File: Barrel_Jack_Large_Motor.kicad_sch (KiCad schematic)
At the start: 9 parts, among them J15 Barrel_Jack, J16 Barrel_Jack, J17 Barrel_Jack, J18 Barrel_Jack, J19 Barrel_Jack, J20 Barrel_Jack, U27 L298N, U28 L298N, U29 L298N

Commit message: motor layout
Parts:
- added F29, F30, F31, F32, F33, F34, F35, F36: Fuse, symbol Device:Fuse
- added J36, J37: Barrel_Jack, symbol Connector:Barrel_Jack
- added U10, U38: PCF8574ATS, Package_SO:SSOP-20_4.4x6.5mm_P0.65mm, symbol Interface_Expansion:PCF8574ATS
- added U37: L298N, Package_TO_SOT_THT:TO-220-15_P2.54x2.54mm_StaggerOdd_Lead4.58mm_Vertical, symbol Driver_Motor:L298N
- added U39: PCA9685PW, Package_SO:TSSOP-28_4.4x9.7mm_P0.65mm, symbol Driver_LED:PCA9685PW
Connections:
- net at J15.1: now also F30.1; no longer U27.14 (OUT4)
- net at J17.1: now also F31.1; no longer U28.14 (OUT4)
- net at U28.10 (IN3): now also U10.19 (P6)
- net at U28.11 (EnB): now also U39.9 (LED3)
- net at U28.12 (IN4): now also U10.20 (P7)
- net at U28.3 (OUT2): now also F32.2; no longer J18.1
- net at U28.5 (IN1): now also U10.16 (P4)
- net at U28.6 (EnA): now also U39.8 (LED2)
- net at U28.7 (IN2): now also U10.17 (P5)
- net at J19.1: now also F34.1; no longer U29.14 (OUT4)
- net at U29.10 (IN3): now also U38.12 (P2)
- net at U29.11 (EnB): now also U39.11 (LED5)
- net at U29.12 (IN4): now also U38.14 (P3)
- net at J20.1: now also F33.1; no longer U29.3 (OUT2)
- net at U29.5 (IN1): now also U38.10 (P0)
- net at U29.6 (EnA): now also U39.10 (LED4)
- net at U29.7 (IN2): now also U38.11 (P1)
- net at J16.1: now also F29.1; no longer U27.3 (OUT2)
- net at U27.10 (IN3): now also U10.12 (P2)
- net at U27.11 (EnB): now also U39.7 (LED1)
- net at U27.12 (IN4): now also U10.14 (P3)
- net at U27.5 (IN1): now also U10.10 (P0)
- net at U27.6 (EnA): now also U39.6 (LED0)
- net at U27.7 (IN2): now also U10.11 (P1)
- new net: F36.1, J36.1
- new net: J36.2, U37.13 (OUT3)
- new net: F36.2, U37.14 (OUT4)
- new net: U37.10 (IN3), U38.19 (P6)
- new net: U37.11 (EnB), U39.13 (LED7)
- new net: U37.12 (IN4), U38.20 (P7)
- new net: J37.2, U37.2 (OUT1)
- new net: F35.2, U37.3 (OUT2)
- new net: U37.5 (IN1), U38.16 (P4)
- new net: U37.6 (EnA), U39.12 (LED6)
- new net: U37.7 (IN2), U38.17 (P5)
- new net: F29.2, U27.3 (OUT2)
- new net: F31.2, U28.14 (OUT4)
- new net: F33.2, U29.3 (OUT2)
- new net: F32.1, J18.1
- new net: F30.2, U27.14 (OUT4)
- new net: F34.2, U29.14 (OUT4)
- new net: F35.1, J37.1
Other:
- moved on the sheet: J15, J16, J17, J18, J19, J20, U27, U28, U29

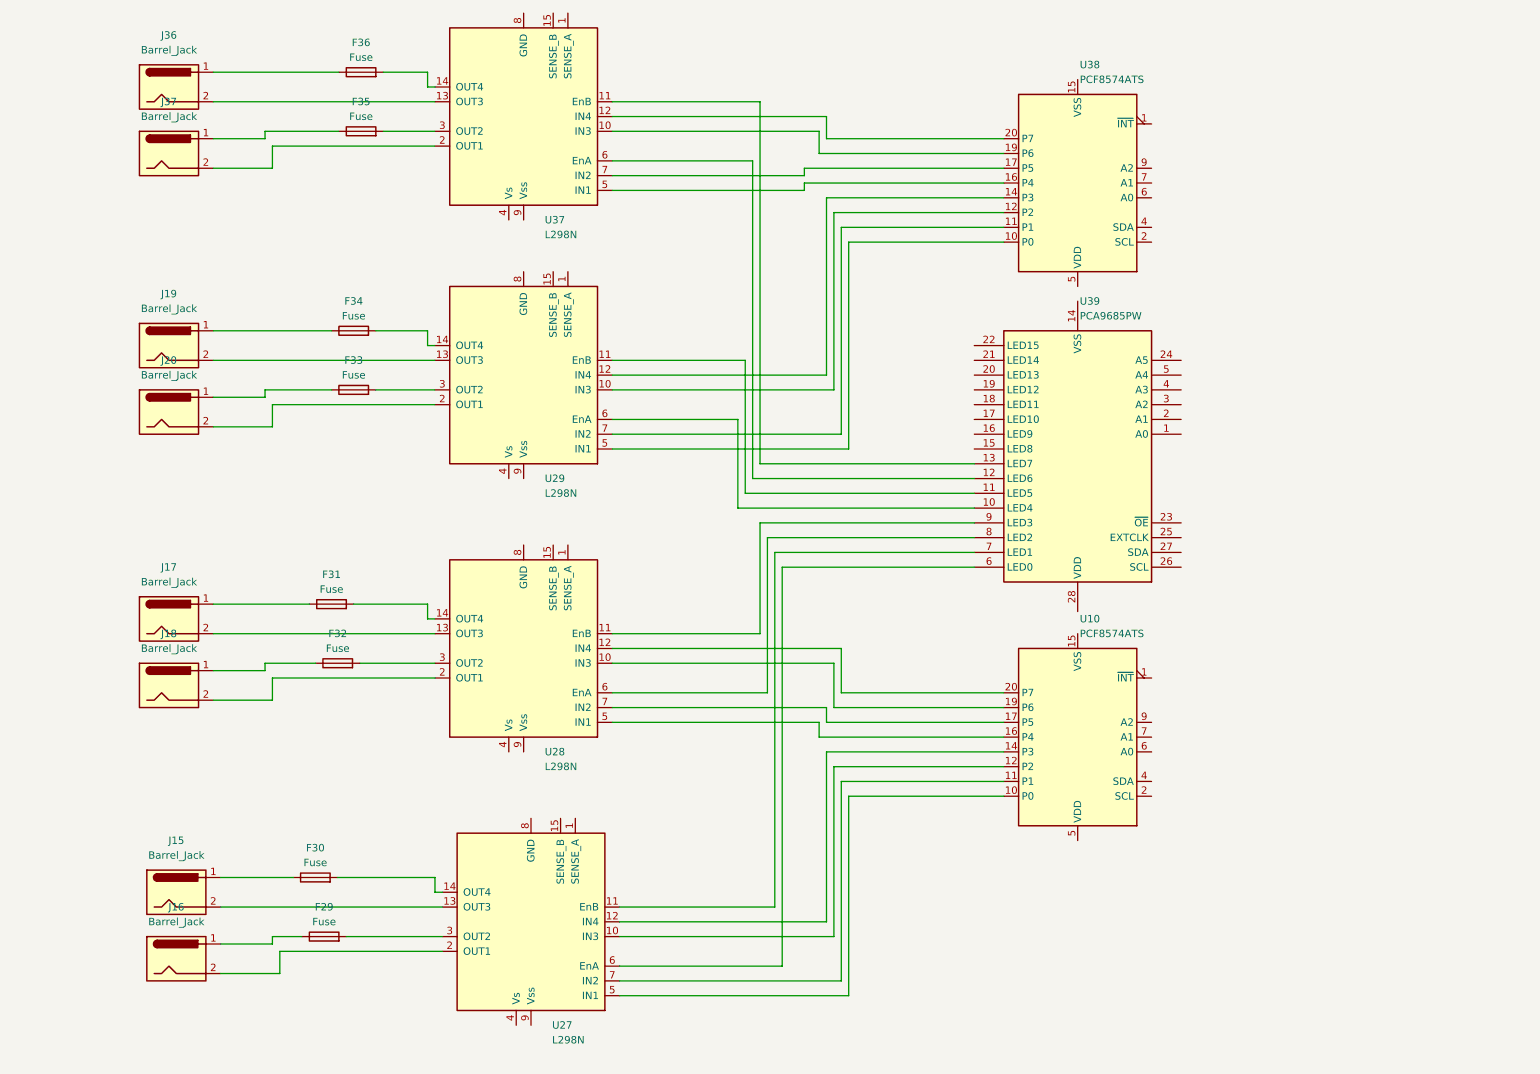
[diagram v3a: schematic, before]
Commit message: placeholders for ethernet and relay inputs
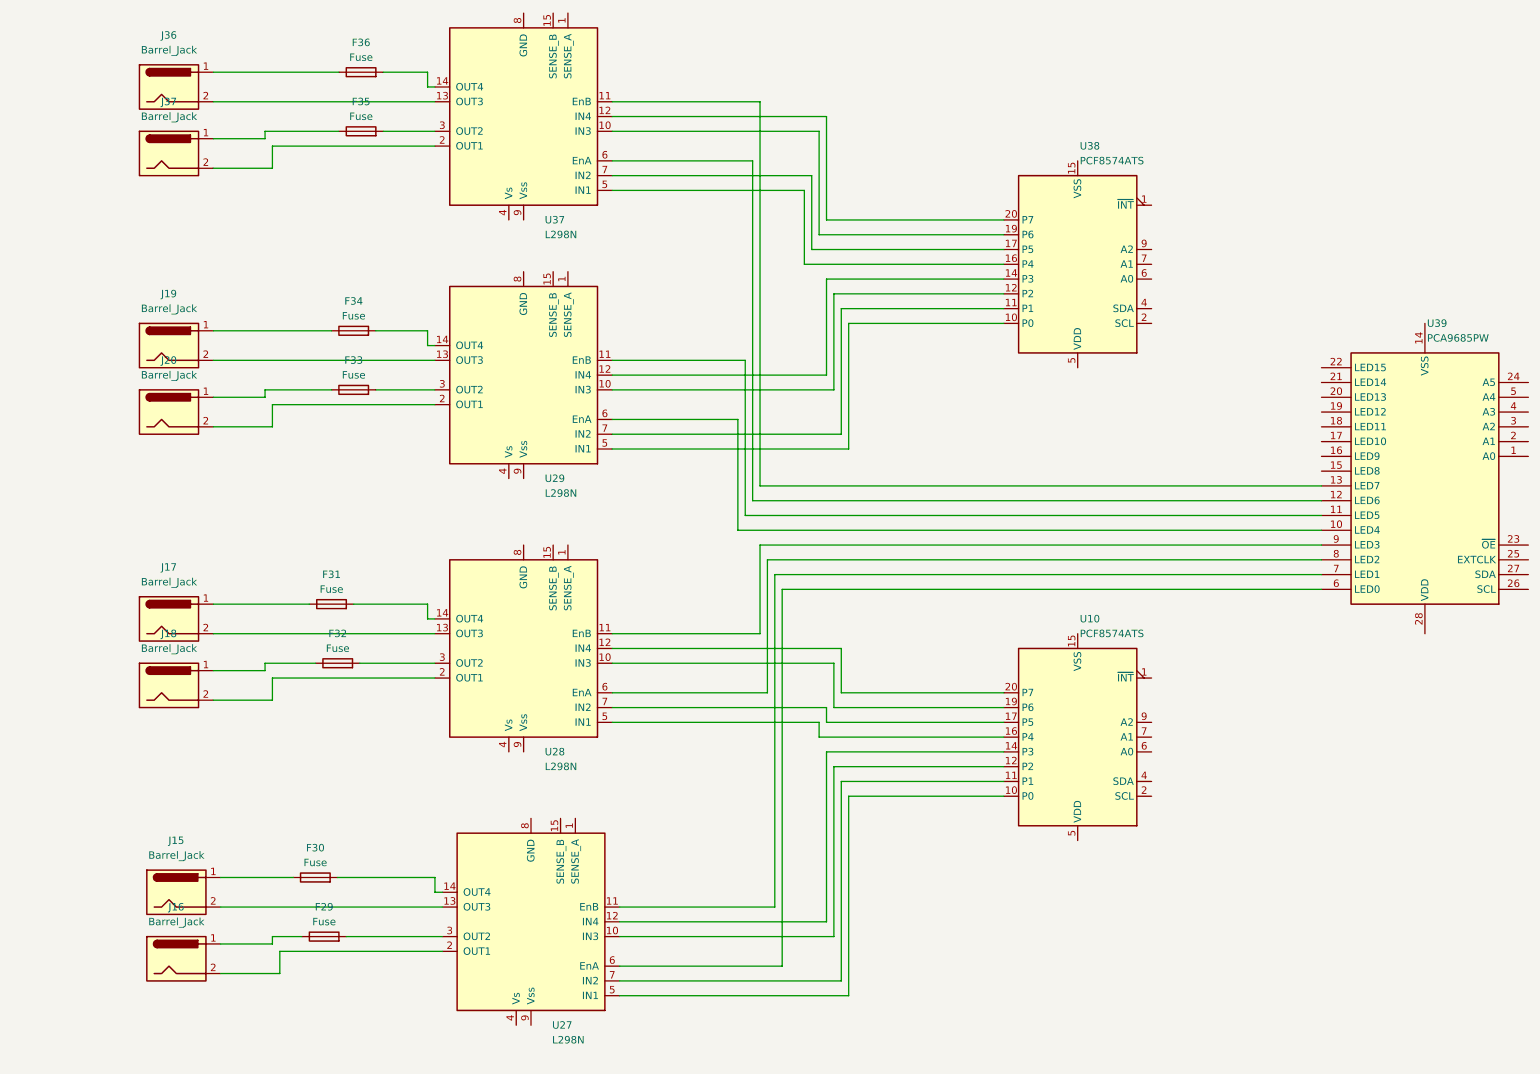
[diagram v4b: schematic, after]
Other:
- moved on the sheet: U38, U39
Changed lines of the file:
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@@
 (kicad_sch (version 20230121) (generator eeschema)
   (paper "A4")
-  (wire (pts (xy 160.02 54.61) (xy 160.02 90.17))
-    (stroke (width 0) (type default))
-  )
-  (wire (pts (xy 120.65 45.72) (xy 153.67 45.72))
-    (stroke (width 0) (type default))
-  )
-  (wire (pts (xy 182.88 107.95) (xy 147.32 107.95))
+  (wire (pts (xy 160.02 68.58) (xy 160.02 90.17))
+    (stroke (width 0) (type default))
+  )
+  (wire (pts (xy 120.65 45.72) (xy 154.94 45.72))
+    (stroke (width 0) (type default))
+  )
+  (wire (pts (xy 242.57 111.76) (xy 147.32 111.76))
     (stroke (width 0) (type default))
   )
@@
     (stroke (width 0) (type default))
   )
-  (wire (pts (xy 146.05 124.46) (xy 146.05 105.41))
+  (wire (pts (xy 146.05 124.46) (xy 146.05 109.22))
     (stroke (width 0) (type default))
   )
@@
     (stroke (width 0) (type default))
   )
-  (wire (pts (xy 149.86 113.03) (xy 149.86 181.61))
+  (wire (pts (xy 149.86 116.84) (xy 149.86 181.61))
     (stroke (width 0) (type default))
   )
@@
     (stroke (width 0) (type default))
   )
-  (wire (pts (xy 182.88 113.03) (xy 149.86 113.03))
-    (stroke (width 0) (type default))
-  )
-  (wire (pts (xy 187.96 46.99) (xy 153.67 46.99))
+  (wire (pts (xy 242.57 116.84) (xy 149.86 116.84))
+    (stroke (width 0) (type default))
+  )
+  (wire (pts (xy 153.67 60.96) (xy 153.67 48.26))
+    (stroke (width 0) (type default))
+  )
+  (wire (pts (xy 153.67 60.96) (xy 187.96 60.96))
     (stroke (width 0) (type default))
   )
@@
     (stroke (width 0) (type default))
   )
-  (wire (pts (xy 187.96 52.07) (xy 158.75 52.07))
+  (wire (pts (xy 187.96 66.04) (xy 158.75 66.04))
     (stroke (width 0) (type default))
   )
@@
     (stroke (width 0) (type default))
   )
-  (wire (pts (xy 146.05 95.25) (xy 146.05 33.02))
+  (wire (pts (xy 146.05 99.06) (xy 146.05 33.02))
     (stroke (width 0) (type default))
   )
@@
     (stroke (width 0) (type default))
   )
-  (wire (pts (xy 120.65 48.26) (xy 153.67 48.26))
-    (stroke (width 0) (type default))
-  )
   (wire (pts (xy 157.48 35.56) (xy 120.65 35.56))
     (stroke (width 0) (type default))
@@
     (stroke (width 0) (type default))
   )
-  (wire (pts (xy 187.96 54.61) (xy 160.02 54.61))
+  (wire (pts (xy 187.96 68.58) (xy 160.02 68.58))
     (stroke (width 0) (type default))
   )
@@
     (stroke (width 0) (type default))
   )
-  (wire (pts (xy 146.05 105.41) (xy 182.88 105.41))
+  (wire (pts (xy 146.05 109.22) (xy 242.57 109.22))
     (stroke (width 0) (type default))
   )
@@
     (stroke (width 0) (type default))
   )
-  (wire (pts (xy 187.96 41.91) (xy 156.21 41.91))
+  (wire (pts (xy 187.96 55.88) (xy 156.21 55.88))
     (stroke (width 0) (type default))
   )
@@
     (stroke (width 0) (type default))
   )
-  (wire (pts (xy 158.75 52.07) (xy 158.75 82.55))
-    (stroke (width 0) (type default))
-  )
-  (wire (pts (xy 157.48 49.53) (xy 157.48 80.01))
+  (wire (pts (xy 158.75 66.04) (xy 158.75 82.55))
+    (stroke (width 0) (type default))
+  )
+  (wire (pts (xy 157.48 63.5) (xy 157.48 80.01))
     (stroke (width 0) (type default))
   )
@@
     (stroke (width 0) (type default))
   )
-  (wire (pts (xy 148.59 110.49) (xy 182.88 110.49))
+  (wire (pts (xy 148.59 114.3) (xy 242.57 114.3))
     (stroke (width 0) (type default))
   )
@@
     (stroke (width 0) (type default))
   )
-  (wire (pts (xy 182.88 95.25) (xy 146.05 95.25))
+  (wire (pts (xy 242.57 99.06) (xy 146.05 99.06))
     (stroke (width 0) (type default))
   )
@@
     (stroke (width 0) (type default))
   )
-  (wire (pts (xy 142.24 102.87) (xy 142.24 87.63))
+  (wire (pts (xy 142.24 106.68) (xy 142.24 87.63))
     (stroke (width 0) (type default))
   )
@@
     (stroke (width 0) (type default))
   )
-  (wire (pts (xy 153.67 44.45) (xy 187.96 44.45))
-    (stroke (width 0) (type default))
-  )
-  (wire (pts (xy 144.78 97.79) (xy 182.88 97.79))
-    (stroke (width 0) (type default))
-  )
-  (wire (pts (xy 143.51 100.33) (xy 143.51 77.47))
+  (wire (pts (xy 154.94 58.42) (xy 187.96 58.42))
+    (stroke (width 0) (type default))
+  )
+  (wire (pts (xy 144.78 101.6) (xy 242.57 101.6))
+    (stroke (width 0) (type default))
+  )
+  (wire (pts (xy 143.51 104.14) (xy 143.51 77.47))
     (stroke (width 0) (type default))
   )
@@
     (stroke (width 0) (type default))
   )
-  (wire (pts (xy 161.29 92.71) (xy 161.29 57.15))
+  (wire (pts (xy 161.29 92.71) (xy 161.29 71.12))
     (stroke (width 0) (type default))
   )
@@
     (stroke (width 0) (type default))
   )
-  (wire (pts (xy 157.48 39.37) (xy 157.48 35.56))
+  (wire (pts (xy 157.48 53.34) (xy 157.48 35.56))
     (stroke (width 0) (type default))
   )
@@
     (stroke (width 0) (type default))
   )
+  (wire (pts (xy 153.67 48.26) (xy 120.65 48.26))
+    (stroke (width 0) (type default))
+  )
   (wire (pts (xy 62.23 44.45) (xy 52.07 44.45))
     (stroke (width 0) (type default))
@@
     (stroke (width 0) (type default))
   )
-  (wire (pts (xy 161.29 57.15) (xy 187.96 57.15))
-    (stroke (width 0) (type default))
-  )
-  (wire (pts (xy 148.59 171.45) (xy 148.59 110.49))
-    (stroke (width 0) (type default))
-  )
-  (wire (pts (xy 144.78 43.18) (xy 144.78 97.79))
+  (wire (pts (xy 161.29 71.12) (xy 187.96 71.12))
+    (stroke (width 0) (type default))
+  )
+  (wire (pts (xy 148.59 171.45) (xy 148.59 114.3))
+    (stroke (width 0) (type default))
+  )
+  (wire (pts (xy 144.78 43.18) (xy 144.78 101.6))
     (stroke (width 0) (type default))
   )
@@
     (stroke (width 0) (type default))
   )
-  (wire (pts (xy 153.67 48.26) (xy 153.67 46.99))
-    (stroke (width 0) (type default))
-  )
   (wire (pts (xy 88.9 30.48) (xy 90.17 30.48))
     (stroke (width 0) (type default))
   )
-  (wire (pts (xy 187.96 49.53) (xy 157.48 49.53))
-    (stroke (width 0) (type default))
-  )
-  (wire (pts (xy 153.67 45.72) (xy 153.67 44.45))
+  (wire (pts (xy 187.96 63.5) (xy 157.48 63.5))
     (stroke (width 0) (type default))
   )
@@
     (stroke (width 0) (type default))
   )
-  (wire (pts (xy 147.32 107.95) (xy 147.32 134.62))
+  (wire (pts (xy 147.32 111.76) (xy 147.32 134.62))
     (stroke (width 0) (type default))
   )
@@
     (stroke (width 0) (type default))
   )
-  (wire (pts (xy 142.24 102.87) (xy 182.88 102.87))
+  (wire (pts (xy 142.24 106.68) (xy 242.57 106.68))
     (stroke (width 0) (type default))
   )
@@
     (stroke (width 0) (type default))
   )
-  (wire (pts (xy 182.88 100.33) (xy 143.51 100.33))
+  (wire (pts (xy 242.57 104.14) (xy 143.51 104.14))
     (stroke (width 0) (type default))
   )
@@
     (stroke (width 0) (type default))
   )
+  (wire (pts (xy 154.94 45.72) (xy 154.94 58.42))
+    (stroke (width 0) (type default))
+  )
   (wire (pts (xy 146.05 33.02) (xy 120.65 33.02))
     (stroke (width 0) (type default))
@@
     (stroke (width 0) (type default))
   )
-  (wire (pts (xy 187.96 39.37) (xy 157.48 39.37))
+  (wire (pts (xy 187.96 53.34) (xy 157.48 53.34))
     (stroke (width 0) (type default))
   )
@@
     (stroke (width 0) (type default))
   )
-  (wire (pts (xy 156.21 41.91) (xy 156.21 38.1))
+  (wire (pts (xy 156.21 55.88) (xy 156.21 38.1))
     (stroke (width 0) (type default))
   )
@@
     )
   )
-  (symbol (lib_id "Driver_LED:PCA9685PW") (at 200.66 95.25 180) (unit 1)
-    (in_bom yes) (on_board yes) (dnp no) (fields_autoplaced)
-    (property "Reference" "U39" (at 201.0059 67.31 0)
-      (effects (font (size 1.27 1.27)) (justify right))
-    )
-    (property "Value" "PCA9685PW" (at 201.0059 69.85 0)
-      (effects (font (size 1.27 1.27)) (justify right))
-    )
-    (property "Footprint" "Package_SO:TSSOP-28_4.4x9.7mm_P0.65mm" (at 200.025 70.485 0)
+  (symbol (lib_id "Driver_LED:PCA9685PW") (at 260.35 99.06 180) (unit 1)
+    (in_bom yes) (on_board yes) (dnp no) (fields_autoplaced)
+    (property "Reference" "U39" (at 260.6959 71.12 0)
+      (effects (font (size 1.27 1.27)) (justify right))
+    )
+    (property "Value" "PCA9685PW" (at 260.6959 73.66 0)
+      (effects (font (size 1.27 1.27)) (justify right))
+    )
+    (property "Footprint" "Package_SO:TSSOP-28_4.4x9.7mm_P0.65mm" (at 259.715 74.295 0)
       (effects (font (size 1.27 1.27)) (justify left) hide)
     )
-    (property "Datasheet" "http://www.nxp.com/docs/en/data-sheet/PCA9685.pdf" (at 210.82 113.03 0)
+    (property "Datasheet" "http://www.nxp.com/docs/en/data-sheet/PCA9685.pdf" (at 270.51 116.84 0)
       (effects (font (size 1.27 1.27)) hide)
     )
@@
     )
   )
-  (symbol (lib_id "Interface_Expansion:PCF8574ATS") (at 200.66 46.99 180) (unit 1)
-    (in_bom yes) (on_board yes) (dnp no) (fields_autoplaced)
-    (property "Reference" "U38" (at 201.0059 26.67 0)
-      (effects (font (size 1.27 1.27)) (justify right))
-    )
-    (property "Value" "PCF8574ATS" (at 201.0059 29.21 0)
-      (effects (font (size 1.27 1.27)) (justify right))
-    )
-    (property "Footprint" "Package_SO:SSOP-20_4.4x6.5mm_P0.65mm" (at 200.66 46.99 0)
-      (effects (font (size 1.27 1.27)) hide)
-    )
-    (property "Datasheet" "http://www.nxp.com/docs/en/data-sheet/PCF8574_PCF8574A.pdf" (at 200.66 46.99 0)
-      (effects (font (size 1.27 1.27)) hide)
-    )
+  (symbol (lib_id "Interface_Expansion:PCF8574ATS") (at 200.66 60.96 180) (unit 1)
+    (in_bom yes) (on_board yes) (dnp no) (fields_autoplaced)
+    (property "Reference" "U38" (at 201.0059 40.64 0)
+      (effects (font (size 1.27 1.27)) (justify right))
+    )
+    (property "Value" "PCF8574ATS" (at 201.0059 43.18 0)
+      (effects (font (size 1.27 1.27)) (justify right))
+    )
+    (property "Footprint" "Package_SO:SSOP-20_4.4x6.5mm_P0.65mm" (at 200.66 60.96 0)
+      (effects (font (size 1.27 1.27)) hide)
+    )
+    (property "Datasheet" "http://www.nxp.com/docs/en/data-sheet/PCF8574_PCF8574A.pdf" (at 200.66 60.96 0)
+      (effects (font (size 1.27 1.27)) hide)
+    )
